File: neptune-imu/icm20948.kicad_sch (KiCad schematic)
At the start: 3 parts, among them U2 ICM-20948

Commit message: session finished
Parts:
- removed U2: ICM-20948, Sensor_Motion:InvenSense_QFN-24_3x3mm_P0.4mm, symbol Sensor_Motion:ICM-20948
- added C11, C12, C13, C16, C17, C18, C19: 100nF, symbol Device:C_Small
- added U2, U4, U6: ICM-20948, ICM-20948:QFN40P300X300X105-24N, symbol neptune-imu-symbols:ICM-20948
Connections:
- net +3.3V: now also C5.1, C12.1, C17.1, U2.13 (VDD), U4.13 (VDD), U6.13 (VDD); no longer C5.2
- net GND: now also C5.2, C11.2, C12.2, C13.2, C16.2, C17.2, C18.2, C19.2, U2.11 (FSYNC), U2.18 (GND), U2.20 (RESV_20), U4.11 (FSYNC), U4.18 (GND), U4.20 (RESV_20), U6.11 (FSYNC), U6.18 (GND), U6.20 (RESV_20); no longer C5.1
- net at C3.1: now also U2.10 (REGOUT)
- new net: C18.1, U6.10 (REGOUT)
- new net: C13.1, U4.10 (REGOUT)
- new net: U2.1 (NC), U2.14 (NC), U2.15 (NC), U2.16 (NC), U2.17 (NC), U2.2 (NC), U2.3 (NC), U2.4 (NC), U2.5 (NC), U2.6 (NC)
- new net: U4.1 (NC), U4.14 (NC), U4.15 (NC), U4.16 (NC), U4.17 (NC), U4.2 (NC), U4.3 (NC), U4.4 (NC), U4.5 (NC), U4.6 (NC)
- new net: U6.1 (NC), U6.14 (NC), U6.15 (NC), U6.16 (NC), U6.17 (NC), U6.2 (NC), U6.3 (NC), U6.4 (NC), U6.5 (NC), U6.6 (NC)
- new net +1V8: C11.1, C16.1, C19.1, U2.8 (VDDIO), U4.8 (VDDIO), U6.8 (VDDIO)
- new net CS1: U2.22 (~{CS})
- new net CS2: U4.22 (~{CS})
- new net CS3: U6.22 (~{CS})
- new net INT_1: U2.12 (INT1)
- new net INT_2: U4.12 (INT1)
- new net INT_3: U6.12 (INT1)
- new net SPI1_MISO: U2.9 (AD0/SDO), U4.9 (AD0/SDO), U6.9 (AD0/SDO)
- new net SPI1_MOSI: U2.24 (SDA/SDI), U4.24 (SDA/SDI), U6.24 (SDA/SDI)
- new net SPI1_SCK: U2.23 (SCL/SCLK), U4.23 (SCL/SCLK), U6.23 (SCL/SCLK)
- no-connect marks 0 -> 9
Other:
- company: (none) -> OnionSAT
- title: (none) -> 9DOF

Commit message: Pécsi folytatja a cuccost
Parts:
- U2, U4, U6: footprint ICM-20948:QFN40P300X300X105-24N -> (none)
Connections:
- net SPI1_MISO renamed MISO_1v8
- net SPI1_MOSI renamed MOSI_1v8
- net SPI1_SCK renamed SCK_1v8
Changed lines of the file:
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@@
 		)
 	)
-	(global_label "SPI1_MOSI"
+	(global_label "MOSI_1v8"
 		(shape input)
 		(at 31.75 55.88 180)
@@
 		)
 		(property "Intersheetrefs" "${INTERSHEET_REFS}"
-			(at 18.9072 55.88 0)
+			(at 19.8144 55.88 0)
 			(effects
 				(font
@@
 		)
 	)
-	(global_label "SPI1_SCK"
+	(global_label "SCK_1v8"
 		(shape input)
 		(at 120.65 50.8 180)
@@
 		)
 		(property "Intersheetrefs" "${INTERSHEET_REFS}"
-			(at 108.6539 50.8 0)
+			(at 109.5611 50.8 0)
 			(effects
 				(font
@@
 		)
 	)
-	(global_label "SPI1_SCK"
+	(global_label "SCK_1v8"
 		(shape input)
 		(at 209.55 50.8 180)
@@
 		)
 		(property "Intersheetrefs" "${INTERSHEET_REFS}"
-			(at 197.5539 50.8 0)
+			(at 198.4611 50.8 0)
 			(effects
 				(font
@@
 		)
 	)
-	(global_label "SPI1_MISO"
+	(global_label "MISO_1v8"
 		(shape output)
 		(at 209.55 48.26 180)
@@
 		)
 		(property "Intersheetrefs" "${INTERSHEET_REFS}"
-			(at 196.7072 48.26 0)
+			(at 197.6144 48.26 0)
 			(effects
 				(font
@@
 		)
 	)
-	(global_label "SPI1_MISO"
+	(global_label "MISO_1v8"
 		(shape output)
 		(at 120.65 48.26 180)
@@
 		)
 		(property "Intersheetrefs" "${INTERSHEET_REFS}"
-			(at 107.8072 48.26 0)
+			(at 108.7144 48.26 0)
 			(effects
 				(font
@@
 		)
 	)
-	(global_label "SPI1_MISO"
+	(global_label "MISO_1v8"
 		(shape output)
 		(at 31.75 50.8 180)
@@
 		)
 		(property "Intersheetrefs" "${INTERSHEET_REFS}"
-			(at 18.9072 50.8 0)
+			(at 19.8144 50.8 0)
 			(effects
 				(font
@@
 		)
 	)
-	(global_label "SPI1_MOSI"
+	(global_label "MOSI_1v8"
 		(shape input)
 		(at 209.55 53.34 180)
@@
 		)
 		(property "Intersheetrefs" "${INTERSHEET_REFS}"
-			(at 196.7072 53.34 0)
+			(at 197.6144 53.34 0)
 			(effects
 				(font
@@
 		)
 	)
-	(global_label "SPI1_SCK"
+	(global_label "SCK_1v8"
 		(shape input)
 		(at 31.75 53.34 180)
@@
 		)
 		(property "Intersheetrefs" "${INTERSHEET_REFS}"
-			(at 19.7539 53.34 0)
+			(at 20.6611 53.34 0)
 			(effects
 				(font
@@
 		)
 	)
-	(global_label "SPI1_MOSI"
+	(global_label "MOSI_1v8"
 		(shape input)
 		(at 120.65 53.34 180)
@@
 		)
 		(property "Intersheetrefs" "${INTERSHEET_REFS}"
-			(at 107.8072 53.34 0)
+			(at 108.7144 53.34 0)
 			(effects
 				(font
@@
 			)
 		)
-		(property "Footprint" "ICM-20948:QFN40P300X300X105-24N"
+		(property "Footprint" ""
 			(at 53.34 53.34 0)
 			(effects
@@
 			)
 		)
-		(property "Footprint" "ICM-20948:QFN40P300X300X105-24N"
+		(property "Footprint" ""
 			(at 142.24 50.8 0)
 			(effects
@@
 			)
 		)
-		(property "Footprint" "ICM-20948:QFN40P300X300X105-24N"
+		(property "Footprint" ""
 			(at 231.14 50.8 0)
 			(effects

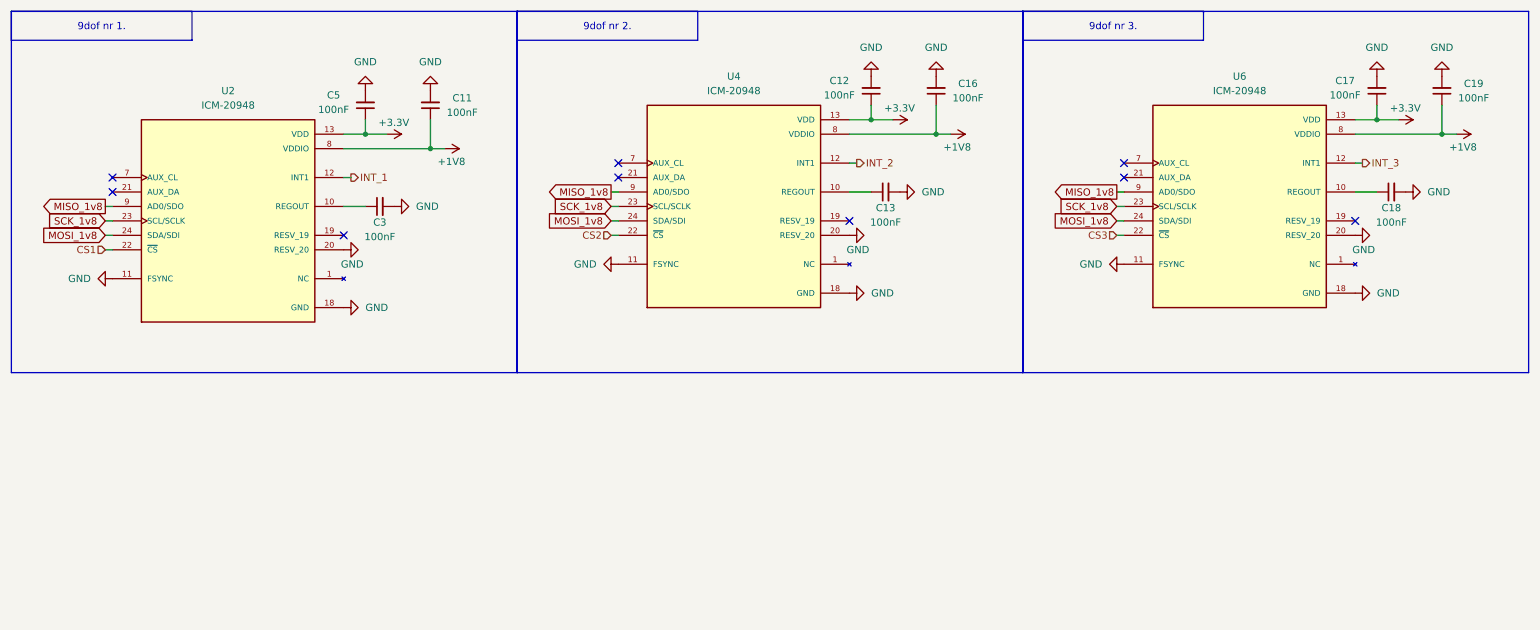
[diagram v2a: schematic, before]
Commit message: level shifter(bss138) + icm20948 + int lines needed
Also some final things like star(orientattion)
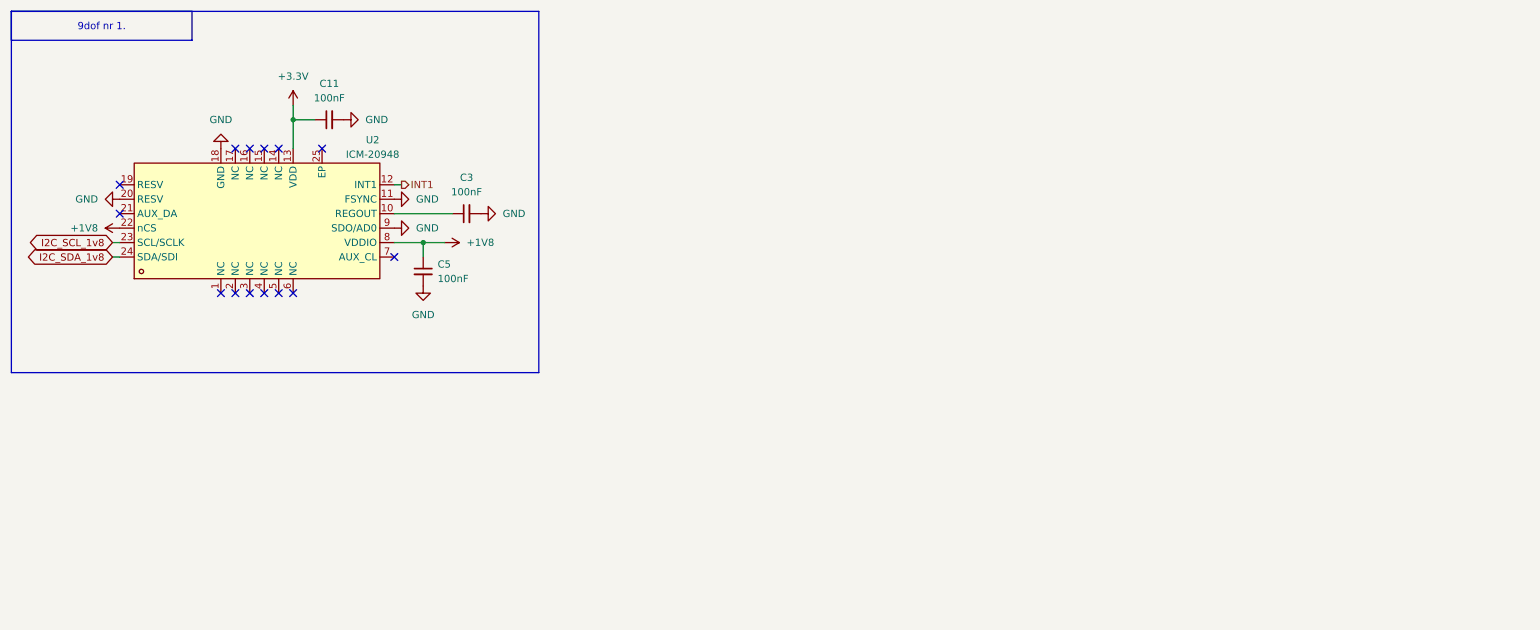
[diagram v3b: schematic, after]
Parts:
- removed C12, C13, C16, C17, C18, C19: 100nF, symbol Device:C_Small
- removed U4, U6: ICM-20948, symbol neptune-imu-symbols:ICM-20948
- U2: footprint (none) -> cigo:QFN-24_L3.0-W3.0-P0.40-BL-EP; Availability In Stock -> (none); Check_prices https://www.snapeda.com/parts/ICM-20948/TDK/view-part/?ref=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 -> (none); Description_1 Accelerometer, Gyroscope, Magnetometer, 9 Axis Sensor I2C, 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 -> (none); LCSC Part (none) -> C726001; MANUFACTURER TDK InvenSense -> (none); MAXIMUM_PACKAGE_HEIGHT 1.05 mm -> (none); MF TDK InvenSense -> (none); MP ICM-20948 -> (none); PARTREV 1.3 -> (none); Package TFQFN-24 TDK InvenSense -> (none); Price None -> (none); STANDARD IPC 7351B -> (none); SnapEDA_Link https://www.snapeda.com/parts/ICM-20948/TDK/view-part/?ref=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 -> (none)
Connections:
- net CS1 is gone; now on net +1V8: U2.22 (nCS)
- net MISO_1v8 is gone; now on net GND: U2.9 (SDO/AD0)
- net +1V8: now also C5.1; no longer C11.1
- net +3.3V: now also C11.1; no longer C5.1
- net INT_1 renamed INT1
- net MOSI_1v8 renamed I2C_SDA_1v8
- net SCK_1v8 renamed I2C_SCL_1v8
- now unconnected: U2.1 (NC), U2.14 (NC), U2.15 (NC), U2.16 (NC), U2.17 (NC), U2.2 (NC), U2.3 (NC), U2.4 (NC), U2.5 (NC), U2.6 (NC)
- no-connect marks 9 -> 14

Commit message: going to school
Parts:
- removed C11, C3, C5: 100nF, symbol Device:C_Small
- removed U2: ICM-20948, cigo:QFN-24_L3.0-W3.0-P0.40-BL-EP, symbol neptune-imu-symbols:ICM-20948
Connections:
- no-connect marks 14 -> 0

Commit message: final
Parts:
- added C11, C3, C5: 100nF, Capacitor_SMD:C_0402_1005Metric, symbol Device:C_Small
- added U2: ICM20948, neptune-imu-footprints:icm20948, symbol neptune-imu-symbols:ICM20948
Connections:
- new net: C11.2, U2.10 (REGOUT)
- new net +1V8: C5.2, U2.22 (nCS), U2.8 (VDDIO)
- new net +3.3V: C3.1, U2.13 (VDD)
- new net 1_INT: U2.12 (INT1)
- new net GND: C11.1, C3.2, C5.1, U2.11 (FSYNC), U2.18 (GND), U2.20 (RESV), U2.9 (SDO/AD0)
- new net SCL: U2.23 (SCL/SCLK)
- new net SDA: U2.24 (SDA/SDI)
- no-connect marks 0 -> 3
